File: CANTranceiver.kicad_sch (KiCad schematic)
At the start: 9 parts, among them U3 IC TRANSCEIVER 1/1 8SO

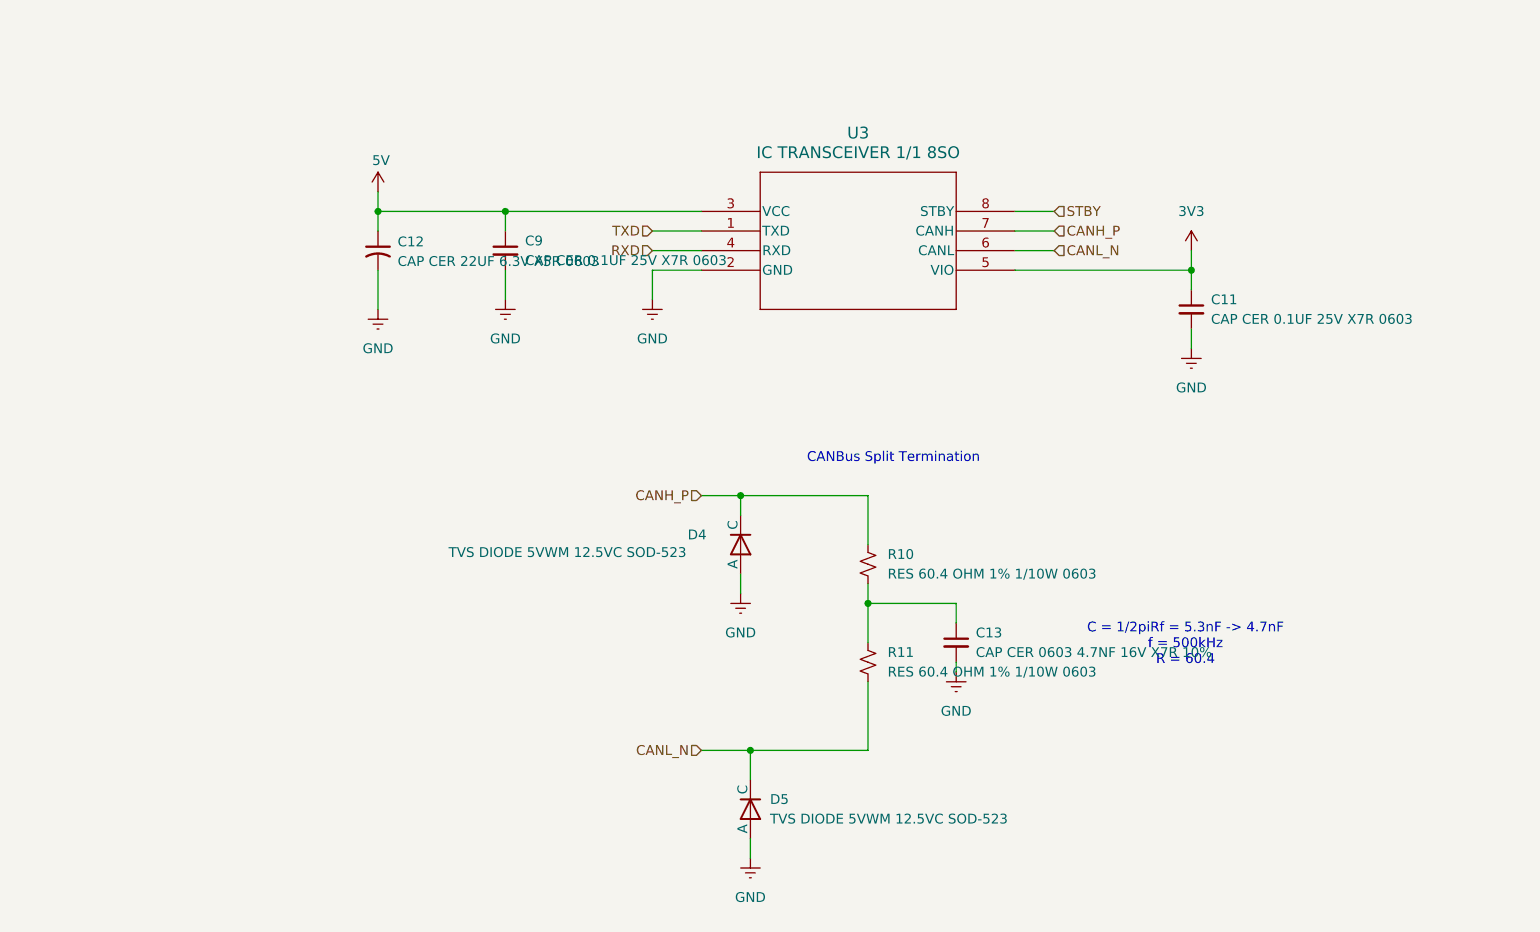
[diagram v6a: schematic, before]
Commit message: cleaned up schematic
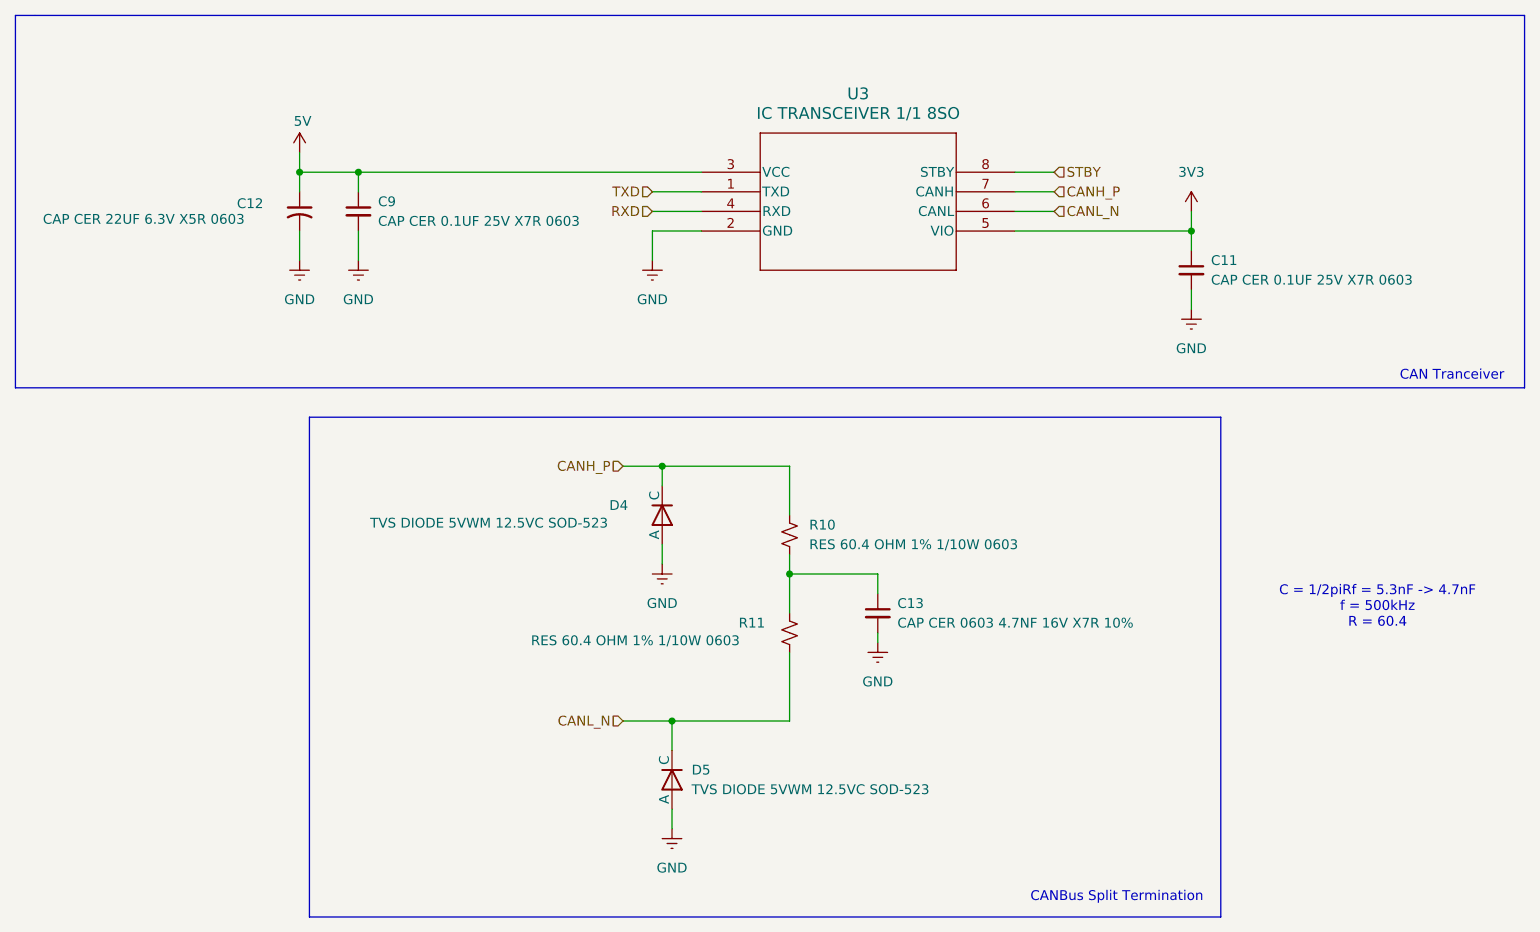
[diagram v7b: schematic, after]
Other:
- note added: "CAN Tranceiver"
- moved on the sheet: C11, C12, C13, C9, D4, D5, R10, R11, U3

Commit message: minor changes
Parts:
- removed C12: CAP CER 22UF 6.3V X5R 0603, Capacitor_SMD:C_0603_1608Metric, symbol Device:C_Small_US
- added C2: CAP ALUM 22UF 20% 16V SMD, footprints:CP_Wurth_WCAP-ASLI-D4L5.5, symbol symbols:D4L5.5_865080340003
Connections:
- net 5V: now also C2.1
- net GND: now also C2.2
